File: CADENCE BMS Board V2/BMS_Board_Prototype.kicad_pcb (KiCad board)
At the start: 4 copper layers, 97 x 97 mm, 174 parts, among them IC1 R5432V407BA, J1 Screw_Terminal_01x02, J10 Conn_01x08, J11 Conn_01x06, J12 Conn_01x02, J13 Conn_01x08, J14 Conn_01x04, J15 Conn_01x08, J2 Conn_01x02, J20 Conn_01x02, J21 Conn_01x02, J28 Banana Socket PWR, J29 Banana Socket VSS, J3 Conn_01x08, J4 Conn_01x02, J5 Conn_01x01_Socket, J6 Conn_01x01_Socket, J7 Conn_01x01_Socket, J8 Conn_01x01_Socket, J9 Conn_01x04, Q1 P-Channel FET, Q10 N-MOS, Q2 60V Enhancement, Q3 60V Enhancement, Q4 60V Enhancement, Q5 Q_NMOS_DSG, Q6 Q_NMOS_DSG, Q7 Q_NMOS_DSG, Q8 N-MOS, Q9 N-MOS, U1 TVS2200DRV, U2 LT8612, U3 LT3652IMSE#PBF, U4 BQ34Z100-R2, U5 MCP9600-E_MX, U7 P82B715DR

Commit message: Updates for banana plug power testing
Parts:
- removed J28: Banana Socket PWR, Connector:Banana_Cliff_FCR7350R_S16N-PC_Horizontal
- removed J29: Banana Socket VSS, Connector:Banana_Cliff_FCR7350B_S16N-PC_Horizontal
- added C55: 3.3uF, Capacitor_SMD:C_0805_2012Metric, F.Cu at (93.5, 32.5)
- added C56: 1uF, Capacitor_SMD:C_0805_2012Metric, F.Cu at (98.8, 36.8)
- added C57: 1uF, Capacitor_SMD:C_0805_2012Metric, F.Cu at (103.3, 33.8)
- added C58: 1uF, Capacitor_SMD:C_0805_2012Metric, F.Cu at (90.0, 40.5)
- added C59: 1uF, Capacitor_SMD:C_0805_2012Metric, F.Cu at (106.3, 33.0)
- added C60: 100nF, Capacitor_SMD:C_0603_1608Metric, F.Cu at (109.5, 33.0)
- added C61: 100nF, Capacitor_SMD:C_0603_1608Metric, F.Cu at (108.0, 33.0)
- added G***: LOGO, LOGO, F.Cu at (112.0, 76.0)
- added J27: USB_C_Receptacle_USB2.0_16P, Connector_USB:USB_C_Receptacle_HRO_TYPE-C-31-M-12, F.Cu at (117.3, 33.5)
- added Q27: Q_PMOS_DGS, Package_TO_SOT_SMD:SOT-23, F.Cu at (95.8, 36.7)
- added Q28: Q_PMOS_DGS, Package_TO_SOT_SMD:SOT-23, F.Cu at (90.0, 37.5)
- added R69: 10K, Resistor_SMD:R_0603_1608Metric_Pad0.98x0.95mm_HandSolder, F.Cu at (100.8, 36.7)
- added R70: 5.1K, Resistor_SMD:R_0603_1608Metric_Pad0.98x0.95mm_HandSolder, F.Cu at (106.2, 29.5)
- added R71: 2.4K, Resistor_SMD:R_0603_1608Metric, F.Cu at (107.0, 27.0)
- added R72: 0, Resistor_SMD:R_0603_1608Metric, F.Cu at (104.2, 31.0)
- added R73: 49.9K, Resistor_SMD:R_0603_1608Metric, F.Cu at (93.0, 36.8)
- added R74: 49.9K, Resistor_SMD:R_0603_1608Metric, F.Cu at (103.2, 28.0)
- added R75: 10K, Resistor_SMD:R_0603_1608Metric, F.Cu at (96.0, 27.2)
- added U11: CYPD3177-24LQ, Package_DFN_QFN:QFN-24-1EP_4x4mm_P0.5mm_EP2.75x2.75mm, F.Cu at (98.8, 31.5)
- moved G*** 11.6 mm to (107.2, 45.2)
- moved Q6 8.92 mm to (103.0, 79.9), turned to 90 degrees
- moved G*** 6.02 mm to (103.5, 85.0)
- moved J20 1.77 mm to (117.2, 44.2)
- moved G*** 0.25 mm to (116.5, 84.1)
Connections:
- D18 pad 2: Net-(D18-A) -> VDC_OUT
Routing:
- net Cell 3-: track 291.1 -> 341.9 mm, vias 88 -> 95
- net VBUS: track 0.00 -> 30.5 mm
- net Net-(Q27-G): track 0.00 -> 26.0 mm, vias 0 -> 2
- net Net-(D18-A): track 22.1 -> 0.00 mm
- net VDC_OUT: track 0.00 -> 20.4 mm
- net CC1: track 0.00 -> 19.3 mm, vias 0 -> 2
- net CC2: track 0.00 -> 19.1 mm, vias 0 -> 2
- net VDDD: track 0.00 -> 13.2 mm, vias 0 -> 2
- net Net-(U11-ISNK_COARSE): track 0.00 -> 9.21 mm
- net Net-(Q6-D): track 24.6 -> 16.8 mm
- net Net-(Q6-G): track 3.47 -> 10.6 mm
- net Net-(Q27-S): track 0.00 -> 6.99 mm
- net Net-(U11-VBUS_MAX): track 0.00 -> 4.37 mm
- net +3.3V: track 112.8 -> 116.4 mm, vias 0 -> 3
- net VBUS_EN: track 0.00 -> 3.16 mm
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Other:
- board text added: "USB C"

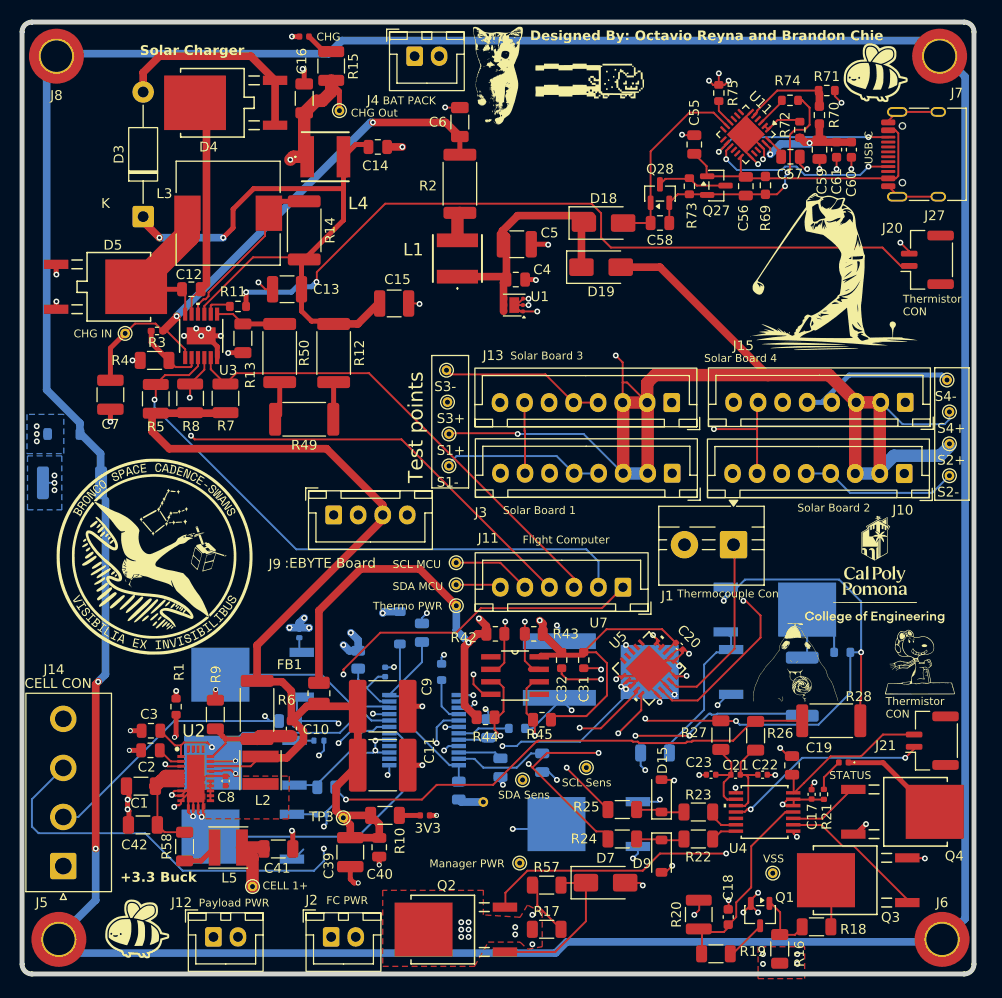
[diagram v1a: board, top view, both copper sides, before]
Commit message: Adding in BMS V2 file for editing
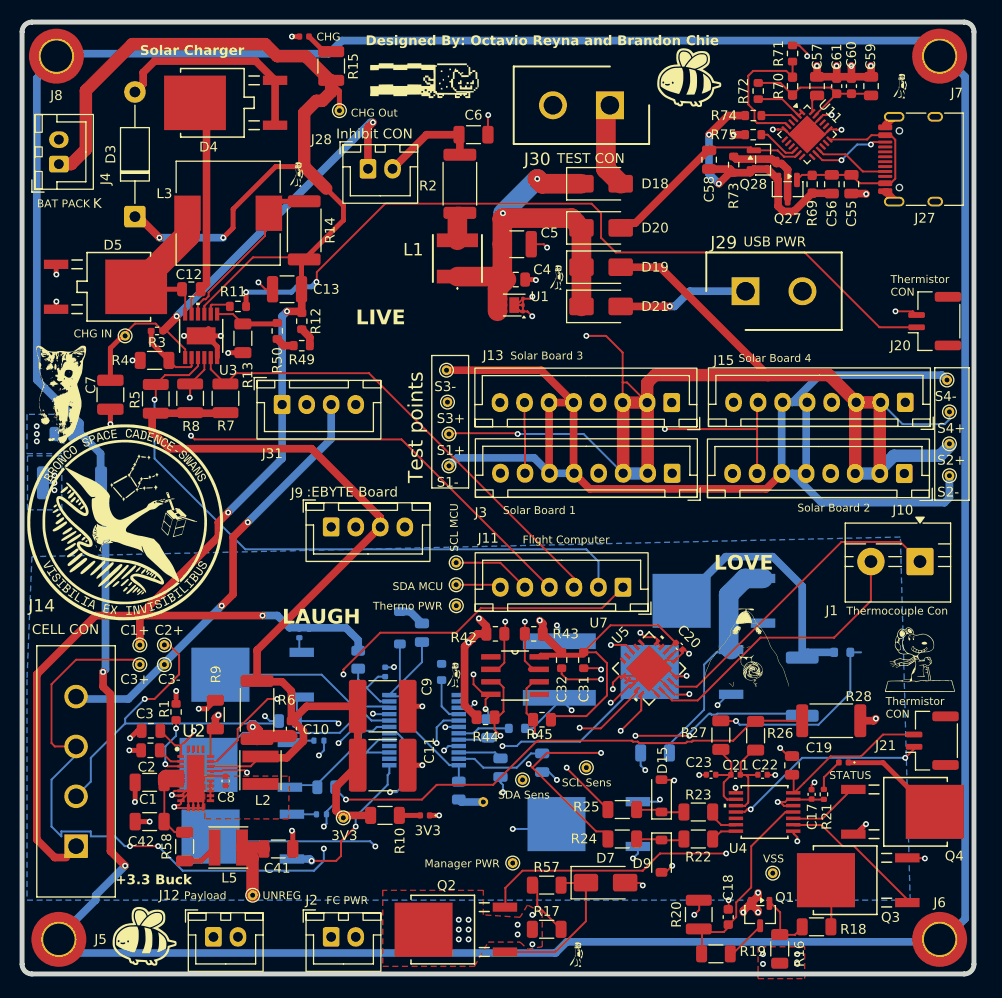
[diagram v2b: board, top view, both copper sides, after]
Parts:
- removed C14, C40: 10nF, Capacitor_SMD:C_0805_2012Metric
- removed C15, C39: 10uF, Capacitor_SMD:C_1210_3225Metric
- removed C16: 4.7uF, Capacitor_SMD:C_1206_3216Metric
- removed FB1: 600, Inductor_SMD:L_1008_2520Metric
- removed the G*** at (112.0, 76.0)
- removed the G*** at (107.2, 45.2)
- removed L4: 4.7u, FNR5040S4R7MT:FNR5040S4R7MT
- added C1+: C1+, TestPoint:TestPoint_THTPad_D1.0mm_Drill0.5mm, F.Cu at (37.0, 83.5)
- added C2+: C2+, TestPoint:TestPoint_THTPad_D1.0mm_Drill0.5mm, F.Cu at (39.5, 83.5)
- added C3+: C3+, TestPoint:TestPoint_THTPad_D1.0mm_Drill0.5mm, F.Cu at (37.0, 85.5)
- added C3-: C3-, TestPoint:TestPoint_THTPad_D1.0mm_Drill0.5mm, F.Cu at (39.5, 85.5)
- added D20: D_Schottky 40v, Diode_SMD:D_SMA, F.Cu at (84.0, 41.0)
- added D21: D_Schottky 40v, Diode_SMD:D_SMA, F.Cu at (84.0, 49.0)
- added G***: LOGO, LOGO, F.Cu at (81.5, 115.0)
- added G***: LOGO, LOGO, F.Cu at (69.0, 86.5)
- added G***: LOGO, LOGO, F.Cu at (53.0, 35.5)
- added G***: LOGO, LOGO, F.Cu at (79.5, 46.0)
- added G***: LOGO, LOGO, F.Cu at (114.5, 26.5)
- added J28: Conn_01x02, Connector_JST:JST_XH_B2B-XH-A_1x02_P2.50mm_Vertical, F.Cu at (60.2, 35.0)
- added J29: Conn_01x02, JST_CON:SHDR2W120P580X500_2X1_790X1380X1460P, F.Cu at (98.7, 47.5)
- added J30: Conn_01x02, JST_CON:SHDR2W120P580X500_2X1_790X1380X1460P, F.Cu at (84.9, 28.5)
- added J31: Conn_01x04, Connector_JST:JST_XH_B4B-XH-A_1x04_P2.50mm_Vertical, F.Cu at (51.5, 59.0)
- C43: footprint Diode_SMD:D_SOD-123 -> Capacitor_SMD:C_0805_2012Metric
- J14: footprint Connector_JST:JST_NV_B04P-NV_1x04_P5.00mm_Vertical -> JST_4Pin_CON:LC04T
- R12, R49, R50: footprint Resistor_SMD:R_2512_6332Metric -> Resistor_SMD:R_0603_1608Metric
- moved G*** 55.1 mm to (29.0, 58.0)
- moved J4 37.9 mm to (28.8, 34.5), turned to 90 degrees
- moved J1 19.1 mm to (116.5, 75.0)
- moved G*** 19.0 mm to (93.0, 25.5)
- moved G*** 16.8 mm to (65.2, 25.7)
- moved C55 16.5 mm to (109.5, 36.5), turned to -90 degrees
- moved Q28 11.1 mm to (100.5, 34.0), turned to 0 degrees
- moved Q6 8.92 mm to (94.2, 79.0), turned to -90 degrees
- moved C56 8.76 mm to (107.5, 36.5)
- moved C59 8.34 mm to (111.5, 26.5), turned to 90 degrees
- moved C58 8.17 mm to (95.0, 34.0), turned to -90 degrees
- moved C57 7.70 mm to (106.0, 26.5), turned to -90 degrees
- moved R49 7.50 mm to (53.5, 53.0)
- moved Q27 7.27 mm to (103.0, 37.0), turned to -90 degrees
- moved G*** 7.27 mm to (32.5, 46.0)
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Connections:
- C1 pad 2: Cell 3- -> Solar1-
- C11 pad 1: Cell 3- -> Solar1-
- C13 pad 1: Net-(D3-K) -> Cell 1+
- C13 pad 2: Cell 3- -> Solar1-
- C17 pad 2: Cell 3- -> Solar1-
- C18 pad 1: Cell 3- -> Solar1-
- C19 pad 1: Cell 3- -> Solar1-
- C2 pad 1: Cell 3- -> Solar1-
- C20 pad 1: Cell 3- -> Solar1-
- C20 pad 2: +3.3V Q -> +3.3V
- C22 pad 1: Cell 3- -> Solar1-
- C23 pad 1: Cell 3- -> Solar1-
- C24 pad 1: Cell 3- -> Solar1-
- C25 pad 2: Cell 3- -> Solar1-
- C26 pad 1: Cell 3- -> Solar1-
- C3 pad 1: Cell 3- -> Solar1-
- C31 pad 1: +3.3V Q -> +3.3V
- C31 pad 2: Cell 3- -> Solar1-
- C32 pad 1: +3.3V Q -> +3.3V
- C32 pad 2: Cell 3- -> Solar1-
- C4 pad 2: Cell 3- -> Solar1-
- C41 pad 1: Cell 1+ -> UNREG
- C41 pad 2: Cell 3- -> Solar1-
- C42 pad 2: Cell 3- -> Solar1-
- C43 pad 2: Cell 3- -> Solar1-
- C5 pad 2: Cell 3- -> Solar1-
- C55 pad 2: Cell 3- -> Solar1-
- C57 pad 1: Cell 3- -> Solar1-
- C59 pad 2: Cell 3- -> Solar1-
- C6 pad 1: Net-(U3-VIN) -> V_mppt_i
- C6 pad 2: Cell 3- -> Solar1-
- C60 pad 2: Cell 3- -> Solar1-
- C61 pad 2: Cell 3- -> Solar1-
- C7 pad 1: Net-(U3-VIN) -> V_mppt_o
- C7 pad 2: Cell 3- -> Solar1-
- C9 pad 1: Cell 3- -> Solar1-
- D15 pad 2: Cell 3- -> Solar1-
- D18 pad 2: VDC_OUT -> TEST_PWR
- D2 pad 1: Cell 3- -> Solar1-
- D3 pad 1: Net-(D3-K) -> Cell 1+
- D5 pad 1: Cell 3- -> Solar1-
- D6 pad 1: Cell 3- -> Solar1-
- D7 pad 2: Cell 3- -> Solar1-
- D9 pad 2: Cell 3- -> Solar1-
- IC1 pad 9: Cell 3- -> Solar1-
- J10 pad 4: Cell 3- -> Solar1-
- J10 pad 5: Cell 3- -> Solar1-
- J10 pad 6: Cell 3- -> Solar1-
- J12 pad 1: Cell 1+ -> UNREG
- J12 pad 2: Cell 3- -> Solar1-
- J13 pad 4: Cell 3- -> Solar1-
- J13 pad 5: Cell 3- -> Solar1-
- J13 pad 6: Cell 3- -> Solar1-
- J15 pad 4: Cell 3- -> Solar1-
- J15 pad 5: Cell 3- -> Solar1-
- J15 pad 6: Cell 3- -> Solar1-
- J2 pad 1: Cell 1+ -> UNREG
- J2 pad 2: Cell 3- -> Solar1-
- J20 pad 2: Cell 3- -> Solar1-
- J27 pad A1: Cell 3- -> Solar1-
- J27 pad A12: Cell 3- -> Solar1-
- J27 pad B1: Cell 3- -> Solar1-
- J27 pad B12: Cell 3- -> Solar1-
- J27 pad SH: Cell 3- -> Solar1-
- J3 pad 4: Cell 3- -> Solar1-
- J3 pad 5: Cell 3- -> Solar1-
- J3 pad 6: Cell 3- -> Solar1-
- J4 pad 2: Cell 3- -> Solar1-
- J9 pad 1: Cell 1+ -> UNREG
- J9 pad 2: Cell 3- -> Solar1-
- J9 pad 4: Cell 3- -> Solar1-
- L5 pad 1: Cell 1+ -> UNREG
- Q1 pad 2: Cell 1+ -> UNREG
- Q2 pad 3: Cell 1+ -> UNREG
- Q3 pad 2: Cell 3- -> Solar1-
- Q4 pad 2: Cell 3- -> Solar1-
- Q5 pad 2: Cell 3- -> Solar1-
- R1 pad 2: Cell 3- -> Solar1-
- R12 pad 1: Net-(D3-K) -> Cell 1+
- R13 pad 2: Cell 3- -> Solar1-
- R14 pad 2: Net-(D3-K) -> Cell 1+
- R16 pad 1: Cell 1+ -> UNREG
- R17 pad 1: Cell 1+ -> UNREG
- R2 pad 2: Net-(U3-VIN) -> V_mppt_i
- R20 pad 2: Cell 3- -> Solar1-
- R3 pad 1: Net-(U3-VIN) -> V_mppt_o
- R31 pad 1: Cell 3- -> Solar1-
- R35 pad 1: Cell 1+ -> UNREG
- R4 pad 2: Cell 3- -> Solar1-
- R42 pad 1: +3.3V Q -> +3.3V
- R43 pad 1: +3.3V Q -> +3.3V
- R44 pad 1: +3.3V Q -> +3.3V
- R45 pad 1: +3.3V Q -> +3.3V
- R59 pad 2: Cell 3- -> Solar1-
- R71 pad 2: Cell 3- -> Solar1-
- R9 pad 2: Cell 3- -> Solar1-
- TP1 pad 1: Cell 1+ -> UNREG
- TP12 pad 1: Cell 3- -> Solar1-
- TP14 pad 1: Cell 3- -> Solar1-
- TP16 pad 1: Cell 3- -> Solar1-
- TP2 pad 1: Net-(U3-VIN) -> V_mppt_o
- TP5 pad 1: Cell 1+ -> UNREG
- TP6 pad 1: Cell 3- -> Solar1-
- TP7 pad 1: +3.3V Q -> +3.3V
- TP8 pad 1: Cell 1+ -> UNREG
- TP9 pad 1: Cell 3- -> Solar1-
- U1 pad 1: Cell 3- -> Solar1-
- U1 pad 2: Cell 3- -> Solar1-
- U1 pad 3: Cell 3- -> Solar1-
- U1 pad 7: Cell 3- -> Solar1-
- U11 pad 19: Cell 3- -> Solar1-
- U11 pad 22: Cell 3- -> Solar1-
- U11 pad 25: Cell 3- -> Solar1-
- U11 pad 6: Cell 3- -> Solar1-
- U2 pad 10: Cell 3- -> Solar1-
- U2 pad 11: Cell 3- -> Solar1-
- U2 pad 12: Cell 3- -> Solar1-
- U2 pad 13: Cell 3- -> Solar1-
- U2 pad 14: Cell 3- -> Solar1-
- U2 pad 29: Cell 3- -> Solar1-
- U2 pad 8: Cell 3- -> Solar1-
- U2 pad 9: Cell 3- -> Solar1-
- U3 pad 1: Net-(U3-VIN) -> V_mppt_o
- U3 pad 13: Cell 3- -> Solar1-
- U3 pad 6: Cell 3- -> Solar1-
- U3 pad 9: Net-(D3-K) -> Cell 1+
- U4 pad 1: Cell 3- -> Solar1-
- U4 pad 8: Cell 3- -> Solar1-
- U5 pad 1: Cell 3- -> Solar1-
- U5 pad 10: Cell 3- -> Solar1-
- U5 pad 13: Cell 3- -> Solar1-
- U5 pad 16: Cell 3- -> Solar1-
- U5 pad 17: Cell 3- -> Solar1-
- U5 pad 18: Cell 3- -> Solar1-
- U5 pad 21: Cell 3- -> Solar1-
- U5 pad 3: Cell 3- -> Solar1-
- U5 pad 5: Cell 3- -> Solar1-
- U5 pad 6: Cell 3- -> Solar1-
- U5 pad 7: Cell 3- -> Solar1-
- U5 pad 8: +3.3V Q -> +3.3V
- U5 pad 9: Cell 3- -> Solar1-
- U7 pad 4: Cell 3- -> Solar1-
- U7 pad 8: +3.3V Q -> +3.3V
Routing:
- net Solar1-: track 0.00 -> 302.6 mm, vias 0 -> 71
- net Cell 3-: track 341.9 -> 92.3 mm, vias 95 -> 6
- net Cell 1+: track 34.9 -> 205.1 mm, vias 23 -> 5
- net +3.3V Q: track 81.9 -> 0.00 mm, vias 3 -> 0
- net Net-(D3-K): track 72.5 -> 0.00 mm, vias 2 -> 0
- net Net-(U3-VIN): track 55.3 -> 0.00 mm, vias 2 -> 0
- net V_mppt_o: track 0.00 -> 49.2 mm, vias 0 -> 2
- net +3.3V: track 116.4 -> 151.6 mm, vias 3 -> 4
- net Cell 3+: track 99.0 -> 118.8 mm, vias 3 -> 5
- net Net-(Q6-G): track 10.6 -> 25.9 mm
- net UNREG: track 0.00 -> 14.7 mm, vias 0 -> 17
- net Net-(J1-Pin_1): track 19.0 -> 32.6 mm
- net USB PWR: track 0.00 -> 13.4 mm, vias 0 -> 1
- net Net-(D18-K): track 28.4 -> 40.1 mm, vias 0 -> 2
- net CC1: track 19.3 -> 7.65 mm, vias 2 -> 0
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- added copper zone on B.Cu, net Solar1-
- added copper zone on In1.Cu, net Solar1-
- added copper zone on F.Cu, net UNREG
- added copper zone on In2.Cu, net UNREG
- removed copper zone on F.Cu, net Cell 1+
- removed copper zone on In2.Cu, net Cell 1+
- removed copper zone on In1.Cu, net Cell 3-
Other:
- board text added: "Inhibit CON"
- board text added: "LAUGH"
- board text added: "LIVE"
- board text added: "LOVE"
- board text added: "Payload"
- board text added: "TEST CON"
- board text added: "UNREG"
- board text added: "USB PWR"
- board text removed: "CELL 1+"
- board text removed: "Payload PWR"
- board text removed: "USB C"
